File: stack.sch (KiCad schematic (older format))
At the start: 6 parts, among them U11 74LS245, U12 74LS173, U13 74LS173, U14 74LS245, U15 74LS173, U16 74LS173

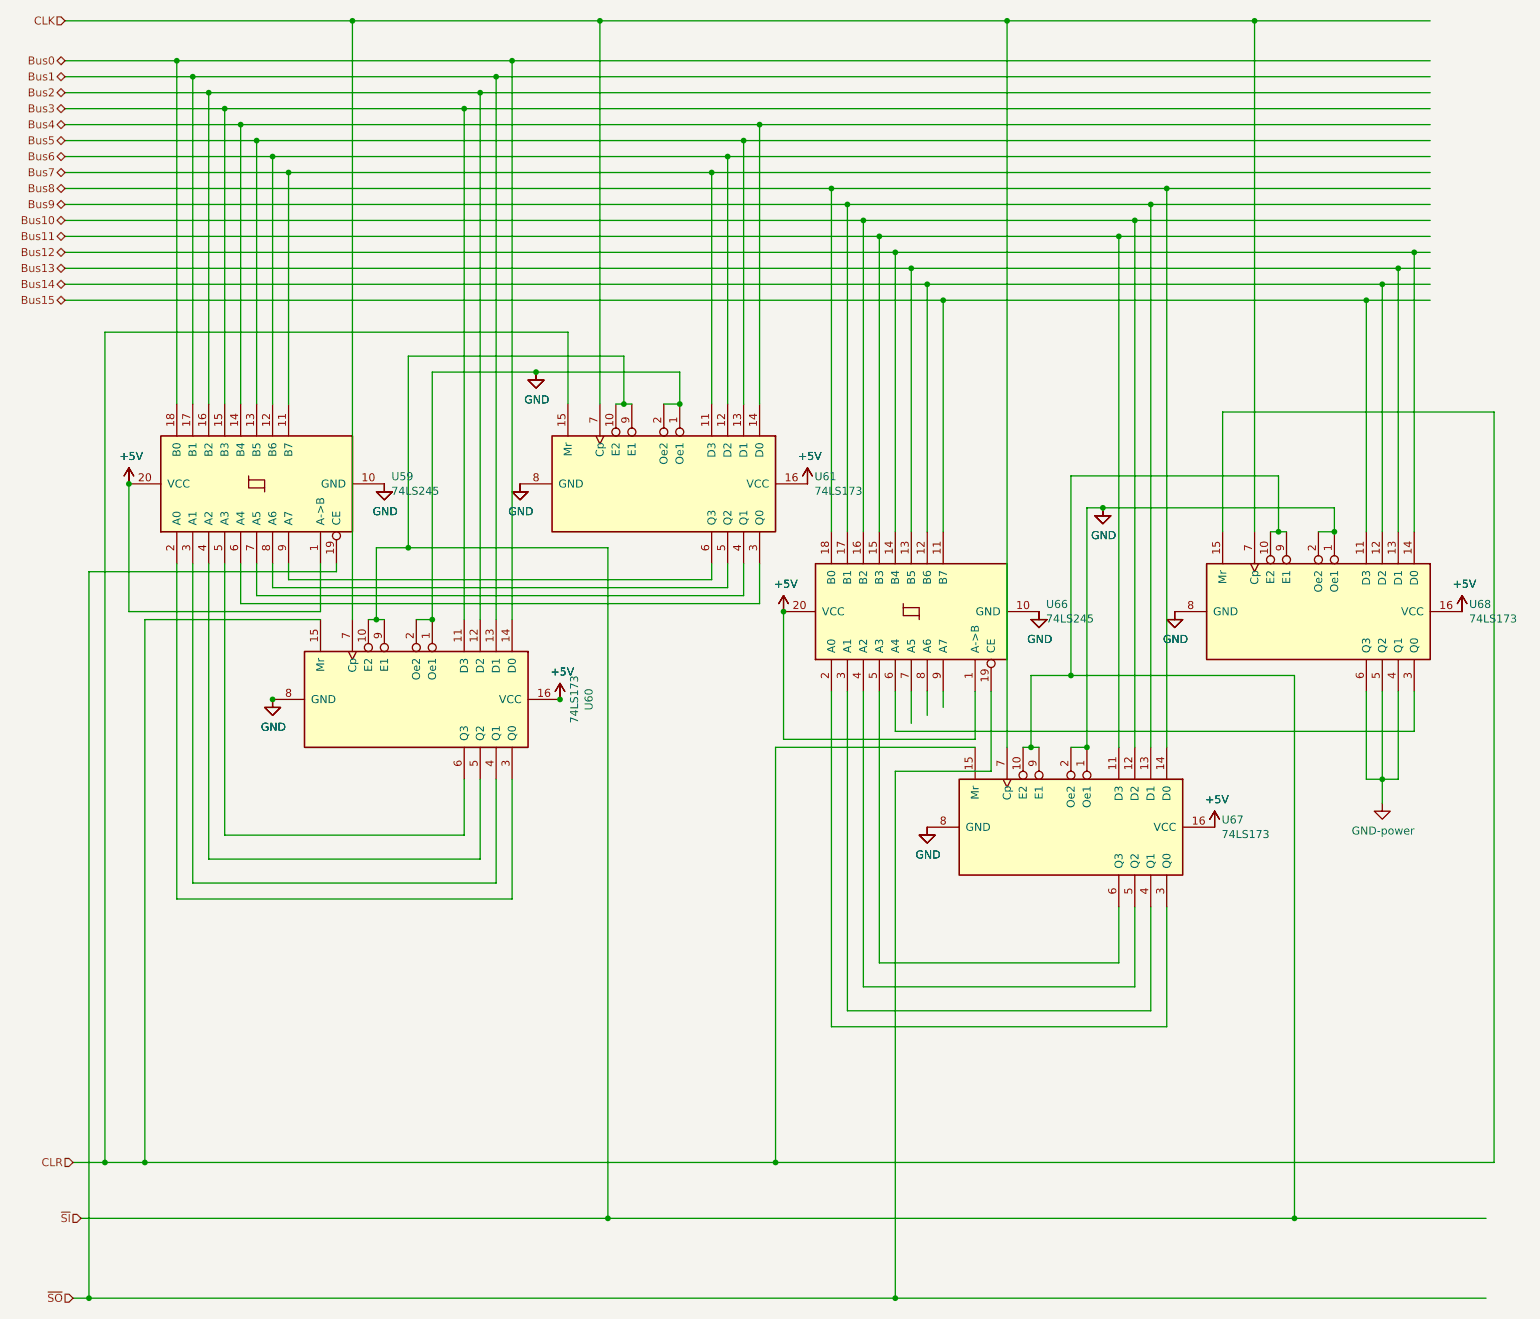
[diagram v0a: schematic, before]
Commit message: Made IR & Stack 12 bits
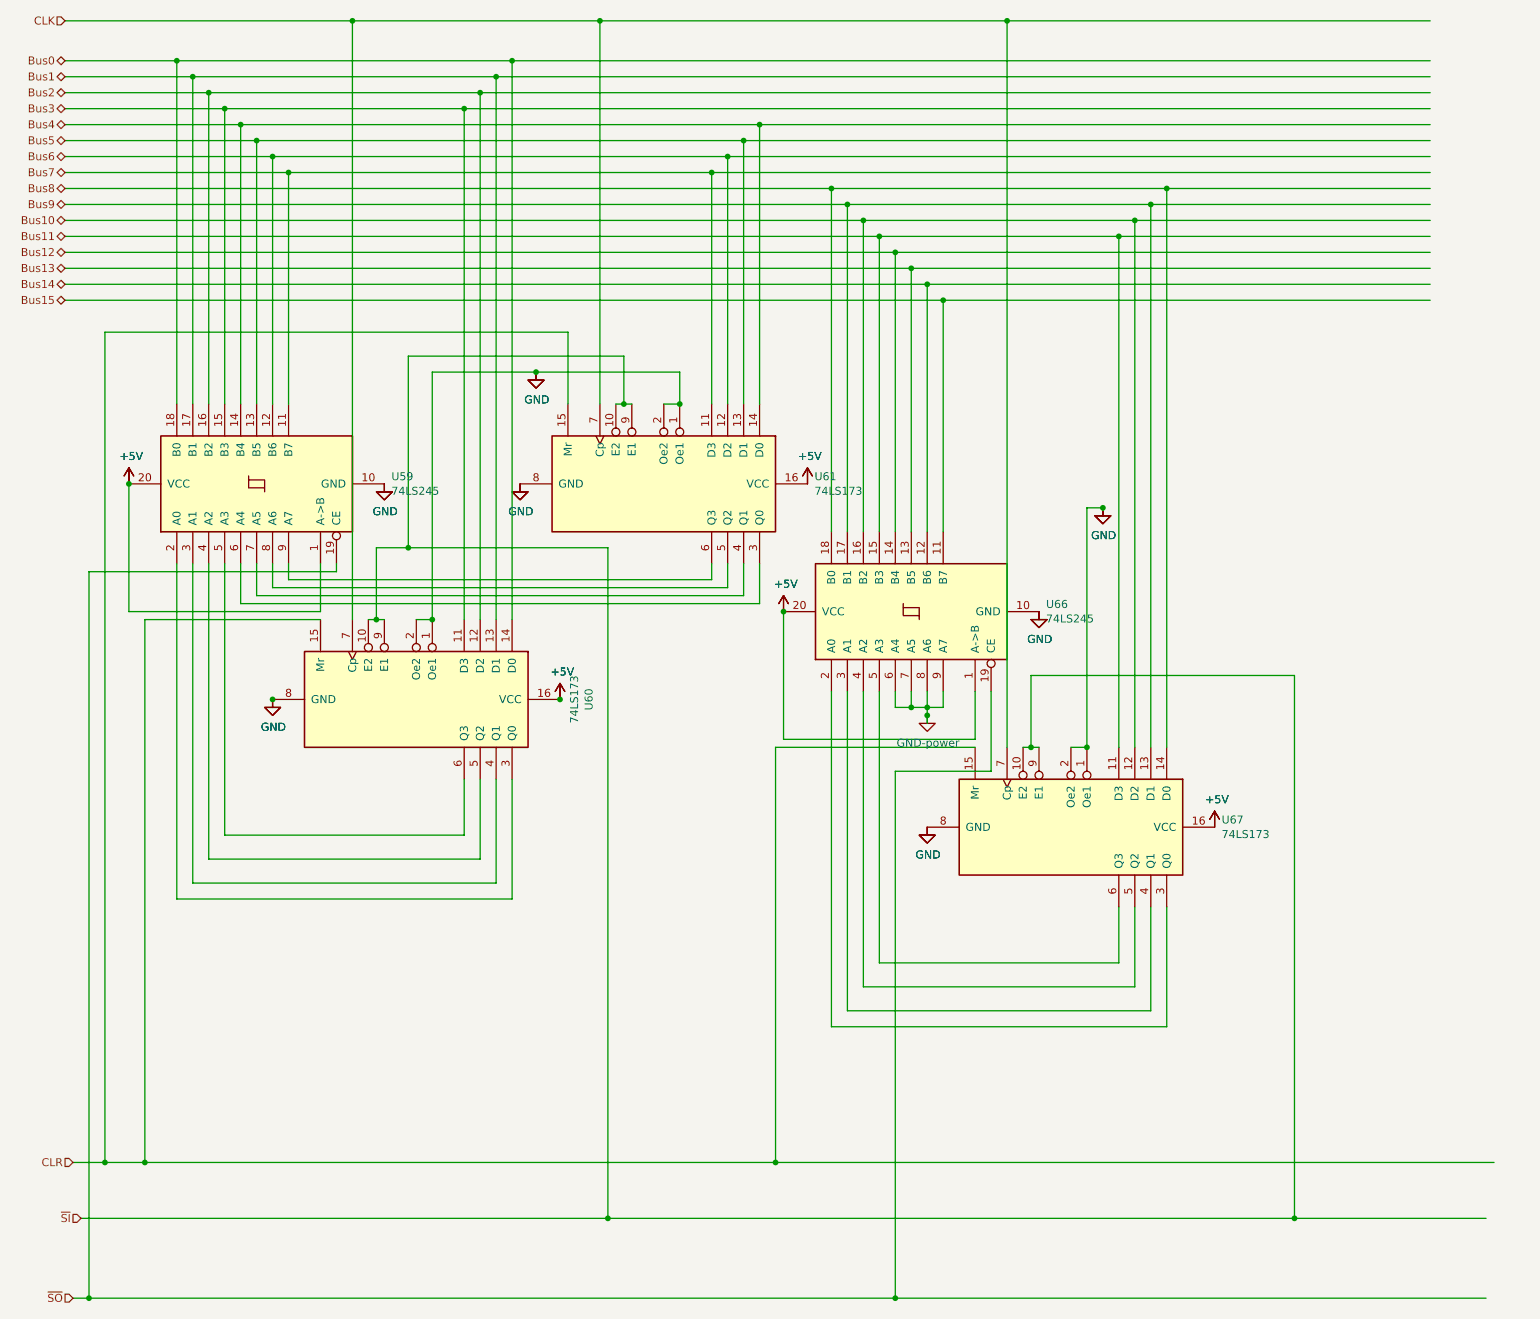
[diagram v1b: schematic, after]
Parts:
- removed U16: 74LS173, Package_DIP:DIP-16_W7.62mm, symbol 16bitCpu-rescue:74LS173-74xx
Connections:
- wire segments 203 -> 178
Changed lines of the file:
@@
 	8000 5150 8000 1850
 Wire Wire Line
-	9750 3800 9750 2050
-Wire Wire Line
-	9650 3800 9650 2150
-Wire Wire Line
-	9550 3800 9550 2250
-Wire Wire Line
-	9450 3800 9450 2350
-Wire Wire Line
 	8200 6900 8200 6150
 Wire Wire Line
@@
 Wire Wire Line
 	6400 6500 6400 4800
-Wire Wire Line
-	6500 4800 6500 5050
-Wire Wire Line
-	9750 5050 9750 4800
-Wire Wire Line
-	6600 4800 6600 5000
-Wire Wire Line
-	6700 4950 6700 4800
-Wire Wire Line
-	6800 4800 6800 4900
 Wire Wire Line
 	7900 5150 7900 1950
@@
 	6400 1950 7900 1950
 Connection ~ 6500 2050
-Wire Wire Line
-	6500 2050 9750 2050
 Connection ~ 6600 2150
-Wire Wire Line
-	6600 2150 9650 2150
 Wire Wire Line
 	6700 3800 6700 2250
 Connection ~ 6700 2250
 Wire Wire Line
-	6700 2250 9550 2250
-Wire Wire Line
 	6800 3800 6800 2350
 Connection ~ 6800 2350
-Wire Wire Line
-	6800 2350 9450 2350
 Connection ~ 7900 1950
 Wire Wire Line
@@
 Wire Wire Line
 	8200 1650 9850 1650
-Connection ~ 9450 2350
-Wire Wire Line
-	9450 2350 9850 2350
-Connection ~ 9550 2250
-Wire Wire Line
-	9550 2250 9850 2250
-Connection ~ 9650 2150
-Wire Wire Line
-	9650 2150 9850 2150
-Connection ~ 9750 2050
-Wire Wire Line
-	9750 2050 9850 2050
 Wire Wire Line
 	8100 6150 8100 6800
@@
 F 3 "" H 7400 4300 50  0001 C CNN
 	1    7400 4300
-	1    0    0    -1
-$EndComp
-$Comp
-L 16bitCpu-rescue:GND-power #PWR?
-U 1 1 616C37A1
-P 8250 4300
-AR Path="/616C37A1" Ref="#PWR?"  Part="1"
-AR Path="/5F67C726/616C37A1" Ref="#PWR044"  Part="1"
-AR Path="/5F70885A/616C37A1" Ref="#PWR?"  Part="1"
-AR Path="/5F733C5E/616C37A1" Ref="#PWR?"  Part="1"
-AR Path="/602D4838/616C37A1" Ref="#PWR?"  Part="1"
-AR Path="/603B00C8/616C37A1" Ref="#PWR?"  Part="1"
-AR Path="/603B766D/616C37A1" Ref="#PWR?"  Part="1"
-AR Path="/5F74778C/616C37A1" Ref="#PWR072"  Part="1"
-AR Path="/5FB94562/616C37A1" Ref="#PWR0206"  Part="1"
-AR Path="/61968B9B/616C37A1" Ref="#PWR0184"  Part="1"
-F 0 "#PWR0184" H 8250 4050 50  0001 C CNN
-F 1 "GND" H 8255 4127 50  0000 C CNN
-F 2 "" H 8250 4300 50  0001 C CNN
-F 3 "" H 8250 4300 50  0001 C CNN
-	1    8250 4300
 	1    0    0    -1
 $EndComp
@@
 $Comp
 L 16bitCpu-rescue:+5V-power #PWR?
-U 1 1 5F7355AB
-P 10050 4300
-AR Path="/5F7355AB" Ref="#PWR?"  Part="1"
-AR Path="/5F67C726/5F7355AB" Ref="#PWR048"  Part="1"
-AR Path="/5F70885A/5F7355AB" Ref="#PWR?"  Part="1"
-AR Path="/5F733C5E/5F7355AB" Ref="#PWR?"  Part="1"
-AR Path="/602D4838/5F7355AB" Ref="#PWR?"  Part="1"
-AR Path="/603B00C8/5F7355AB" Ref="#PWR?"  Part="1"
-AR Path="/603B766D/5F7355AB" Ref="#PWR?"  Part="1"
-AR Path="/5F74778C/5F7355AB" Ref="#PWR076"  Part="1"
-AR Path="/5FB94562/5F7355AB" Ref="#PWR0210"  Part="1"
-AR Path="/61968B9B/5F7355AB" Ref="#PWR0192"  Part="1"
-F 0 "#PWR0192" H 10050 4150 50  0001 C CNN
-F 1 "+5V" H 10065 4473 50  0000 C CNN
-F 2 "" H 10050 4300 50  0001 C CNN
-F 3 "" H 10050 4300 50  0001 C CNN
-	1    10050 4300
-	1    0    0    -1
-$EndComp
-$Comp
-L 16bitCpu-rescue:+5V-power #PWR?
 U 1 1 616C37AB
 P 5950 3500
@@
 Wire Wire Line
 	7700 3650 7800 3650
-Wire Wire Line
-	9250 3650 9250 3800
 Connection ~ 7700 5150
-Wire Wire Line
-	9150 3800 9250 3800
-Connection ~ 9250 3800
 $Comp
 L 16bitCpu-rescue:GND-power #PWR?
@@
 Connection ~ 7800 3650
 Wire Wire Line
-	7800 3650 9250 3650
-Wire Wire Line
 	7200 5150 7200 600
-Wire Wire Line
-	7200 600  8750 600
 Connection ~ 7200 600
-Wire Wire Line
-	8750 3800 8750 600
-Connection ~ 8750 600
-Wire Wire Line
-	8750 600  9850 600
 Wire Wire Line
 	4650 3000 4650 600
@@
 Connection ~ 5750 7750
 Wire Wire Line
-	8550 3800 8550 3050
-Wire Wire Line
-	8550 3050 10250 3050
-Wire Wire Line
 	5750 7750 10250 7750
 Wire Wire Line
@@
 Wire Wire Line
 	7350 5150 7350 4700
-Wire Wire Line
-	7350 4700 7600 4700
-Wire Wire Line
-	7600 4700 7600 3450
-Wire Wire Line
-	7600 3450 8900 3450
-Wire Wire Line
-	8900 3450 8900 3800
-Wire Wire Line
-	8900 3800 8950 3800
 Connection ~ 7350 5150
 Wire Wire Line
 	7350 5150 7400 5150
-Wire Wire Line
-	8900 3800 8850 3800
-Connection ~ 8900 3800
 Wire Wire Line
 	3200 4350 3250 4350
@@
 	4700 8100 9000 8100
 Wire Wire Line
-	7600 4700 9000 4700
-Wire Wire Line
 	9000 4700 9000 8100
-Connection ~ 7600 4700
 Connection ~ 9000 8100
 Wire Wire Line
@@
 $EndComp
 $Comp
-L 16bitCpu-rescue:74LS173-74xx U?
-U 1 1 5F73559F
-P 9150 4300
-AR Path="/5F73559F" Ref="U?"  Part="1"
-AR Path="/5F67C726/5F73559F" Ref="U16"  Part="1"
-AR Path="/5F70885A/5F73559F" Ref="U?"  Part="1"
-AR Path="/5F733C5E/5F73559F" Ref="U?"  Part="1"
-AR Path="/602D4838/5F73559F" Ref="U?"  Part="1"
-AR Path="/603B00C8/5F73559F" Ref="U?"  Part="1"
-AR Path="/603B766D/5F73559F" Ref="U?"  Part="1"
-AR Path="/5F74778C/5F73559F" Ref="U22"  Part="1"
-AR Path="/5FB94562/5F73559F" Ref="U68"  Part="1"
-AR Path="/61968B9B/5F73559F" Ref="U68"  Part="1"
-F 0 "U68" V 9104 5244 50  0000 L CNN
-F 1 "74LS173" V 9195 5244 50  0000 L CNN
-F 2 "Package_DIP:DIP-16_W7.62mm" H 9150 4300 50  0001 C CNN
-F 3 "http://www.ti.com/lit/gpn/sn74LS173" H 9150 4300 50  0001 C CNN
-	1    9150 4300
-	0    1    1    0
-$EndComp
-$Comp
 L 16bitCpu-rescue:GND-power #PWR?
 U 1 1 5F6AAC29
@@
 F 3 "" H 7400 4300 50  0001 C CNN
 	1    7400 4300
-	1    0    0    -1
-$EndComp
-$Comp
-L 16bitCpu-rescue:GND-power #PWR?
-U 1 1 5F6AAC2F
-P 8250 4300
-AR Path="/5F6AAC2F" Ref="#PWR?"  Part="1"
-AR Path="/5F67C726/5F6AAC2F" Ref="#PWR043"  Part="1"
-AR Path="/5F70885A/5F6AAC2F" Ref="#PWR?"  Part="1"
-AR Path="/5F733C5E/5F6AAC2F" Ref="#PWR?"  Part="1"
-AR Path="/602D4838/5F6AAC2F" Ref="#PWR?"  Part="1"
-AR Path="/603B00C8/5F6AAC2F" Ref="#PWR?"  Part="1"
-AR Path="/603B766D/5F6AAC2F" Ref="#PWR?"  Part="1"
-AR Path="/5F74778C/5F6AAC2F" Ref="#PWR071"  Part="1"
-AR Path="/5FB94562/5F6AAC2F" Ref="#PWR0205"  Part="1"
-AR Path="/61968B9B/5F6AAC2F" Ref="#PWR0197"  Part="1"
-F 0 "#PWR0197" H 8250 4050 50  0001 C CNN
-F 1 "GND" H 8255 4127 50  0000 C CNN
-F 2 "" H 8250 4300 50  0001 C CNN
-F 3 "" H 8250 4300 50  0001 C CNN
-	1    8250 4300
 	1    0    0    -1
 $EndComp
@@
 F 3 "" H 8500 5650 50  0001 C CNN
 	1    8500 5650
-	1    0    0    -1
-$EndComp
-$Comp
-L 16bitCpu-rescue:+5V-power #PWR?
-U 1 1 616C3799
-P 10050 4300
-AR Path="/616C3799" Ref="#PWR?"  Part="1"
-AR Path="/5F67C726/616C3799" Ref="#PWR047"  Part="1"
-AR Path="/5F70885A/616C3799" Ref="#PWR?"  Part="1"
-AR Path="/5F733C5E/616C3799" Ref="#PWR?"  Part="1"
-AR Path="/602D4838/616C3799" Ref="#PWR?"  Part="1"
-AR Path="/603B00C8/616C3799" Ref="#PWR?"  Part="1"
-AR Path="/603B766D/616C3799" Ref="#PWR?"  Part="1"
-AR Path="/5F74778C/616C3799" Ref="#PWR075"  Part="1"
-AR Path="/5FB94562/616C3799" Ref="#PWR0211"  Part="1"
-AR Path="/61968B9B/616C3799" Ref="#PWR0206"  Part="1"
-F 0 "#PWR0206" H 10050 4150 50  0001 C CNN
-F 1 "+5V" H 10065 4473 50  0000 C CNN
-F 2 "" H 10050 4300 50  0001 C CNN
-F 3 "" H 10050 4300 50  0001 C CNN
-	1    10050 4300
 	1    0    0    -1
 $EndComp
@@
 Connection ~ 4400 4850
 Connection ~ 2600 4850
-Wire Wire Line
-	10250 3050 10250 7750
 $Comp
 L 16bitCpu-rescue:74LS173-74xx U?
@@
 Bus15
 Wire Wire Line
-	6500 5050 9750 5050
-Wire Wire Line
 	6100 6900 8200 6900
 Wire Wire Line
@@
 Wire Wire Line
 	2300 5700 3800 5700
-Wire Wire Line
-	9450 5350 9550 5350
-Wire Wire Line
-	9550 4800 9550 5350
-Wire Wire Line
-	9450 4800 9450 5350
-Wire Wire Line
-	9650 5350 9550 5350
-Wire Wire Line
-	9650 4800 9650 5350
-Connection ~ 9550 5350
-Wire Wire Line
-	9550 5350 9550 5500
 $Comp
 L 16bitCpu-rescue:GND-power #PWR0211
 U 1 1 60C78EFB
-P 9550 5500
-F 0 "#PWR0211" H 9550 5250 50  0001 C CNN
-F 1 "GND-power" H 9555 5327 50  0000 C CNN
-F 2 "" H 9550 5500 50  0001 C CNN
-F 3 "" H 9550 5500 50  0001 C CNN
-	1    9550 5500
-	1    0    0    -1
-$EndComp
+P 6700 4950
+F 0 "#PWR0211" H 6700 4700 50  0001 C CNN
+F 1 "GND-power" H 6705 4777 50  0000 C CNN
+F 2 "" H 6700 4950 50  0001 C CNN
+F 3 "" H 6700 4950 50  0001 C CNN
+	1    6700 4950
+	1    0    0    -1
+$EndComp
+Wire Wire Line
+	6500 2050 9850 2050
+Wire Wire Line
+	6600 2150 9850 2150
+Wire Wire Line
+	6700 2250 9850 2250
+Wire Wire Line
+	6800 2350 9850 2350
+Wire Wire Line
+	7200 600  9850 600
+Wire Wire Line
+	7350 4700 9000 4700
+Wire Wire Line
+	6600 4800 6600 4900
+Wire Wire Line
+	6600 4900 6700 4900
+Wire Wire Line
+	6700 4900 6700 4800
+Wire Wire Line
+	6800 4800 6800 4900
+Wire Wire Line
+	6800 4900 6700 4900
+Connection ~ 6700 4900
+Wire Wire Line
+	6700 4900 6700 4950
+Connection ~ 6700 4950
+Wire Wire Line
+	6700 4950 6700 5000
+Wire Wire Line
+	6500 4800 6500 4900
+Wire Wire Line
+	6500 4900 6600 4900
+Connection ~ 6600 4900
 $EndSCHEMATC
